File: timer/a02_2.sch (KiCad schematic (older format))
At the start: 6 parts, among them U11 74HC27, U12 74HC02, U13 74HC02, U14 74HC02, U15 74HC02, U16 74HC02

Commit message: Added the start/stop logic to timer page A02-2, and introduced a new part, 74LVC07, that I think will be the solution for open drain things
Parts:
- added R1: 5k, symbol R
- added unit 3 of U11
- added unit 3 of U16
- added unit 4 of U16
- added U19: 74HC27, symbol 74HC27
- added U20: 74LVC07, symbol 74LVC07
- added U21: 74HC04, symbol 74HC04
- added U22, U23: 74HC02, symbol 74HC02
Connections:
- net GND: now also U11.7 (GND), U16.7 (GND), U16.7 (GND), U19.7 (GND), U19.7 (GND), U19.7 (GND), U20.7 (GND), U20.7 (GND), U21.7 (GND), U21.7 (GND), U21.7 (GND), U21.7 (GND), U21.7 (GND), U21.7 (GND), U22.7 (GND), U22.7 (GND), U22.7 (GND), U23.7 (GND), U23.7 (GND), U23.7 (GND), U23.7 (GND)
- net VCC: now also R1.1, U11.14 (VCC), U16.14 (VCC), U16.14 (VCC), U19.14 (VCC), U19.14 (VCC), U19.14 (VCC), U20.14 (VCC), U20.14 (VCC), U21.14 (VCC), U21.14 (VCC), U21.14 (VCC), U21.14 (VCC), U21.14 (VCC), U21.14 (VCC), U22.14 (VCC), U22.14 (VCC), U22.14 (VCC), U23.14 (VCC), U23.14 (VCC), U23.14 (VCC), U23.14 (VCC)
- new net: U19.12, U20.1
- new net: R1.2, U11.10, U16.8, U20.2, U20.4, U21.1
- new net: U19.6, U20.3
- new net: U16.10, U19.5
- new net: U16.12, U21.2
- new net: U11.8, U23.2
- new net: U19.10, U21.4
- new net: U19.8, U23.8
- new net: U16.13, U23.6
- new net: U22.1, U23.12
- new net: U23.1, U23.5
- new net: U23.10, U23.11
- new net: U22.9, U23.13, U23.9
- new net ALGA: U19.2
- new net EVNSET/: U11.11, U16.11, U19.11, U22.2
- new net GOJ1: U16.9
- new net GOJAM: U21.6, U21.9
- new net GOJAM/: U21.5, U22.4
- new net MGOJAM: U21.8
- new net MSTP: U21.3, U22.3
- new net MSTPIT/: U21.12
- new net MSTRTP: U19.13
- new net SBY: U19.1
- new net STOP: U21.10, U21.13
- new net STOP/: U21.11, U22.10
- new net STOPA: U22.6, U22.8, U23.3, U23.4
- new net STRT1: U19.3
- new net STRT2: U19.4, U22.5
- new net T12DC/: U11.9, U19.9
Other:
- note added: "First stage of the scaler. This should maybe be moved to the scaler module?\nIt probably makes more sense there."
- note added: "Start/Stop Logic"
- note added: "TODO: Add descriptive local net names to this for debugging"

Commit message: Filled out the rest of page A03-1. At the very least, it appears to be properly handling the GOJAM condition. Haven't looked much at non-GOJAM behavior. I also exposed T01..T12 and T01/..T12/ as outputs of the timer module. I'm going to need a bigger (or another) connector there soon
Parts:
- U23: Initial (none) -> 1
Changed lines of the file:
@@
 F 2 "" H 13450 4550 60  0000 C CNN
 F 3 "" H 13450 4550 60  0000 C CNN
+F 4 "1" H 13700 4550 60  0000 C CIN "Initial"
 	1    13450 4550
 	1    0    0    -1
@@
 F 2 "" H 13450 5850 60  0000 C CNN
 F 3 "" H 13450 5850 60  0000 C CNN
+F 4 "1" H 13700 5850 60  0000 C CIN "Initial"
 	3    13450 5850
 	1    0    0    -1

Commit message: Renamed components in the timer module to fit the new numbering scheme (module_number * 1000 + part number), and updated initial conditions to make simulation happy again after fixes
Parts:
- renumbered R1 to R2001, U11 to U2011, U12 to U2012, U13 to U2013, U14 to U2014, U15 to U2015, U16 to U2016, U19 to U2019, U21 to U2021, U22 to U2022, U23 to U2023

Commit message: Added the 'stage' bit of the Stage Branch Decoder module, and cleaned up a lot of initial conditions (still probably a lot to be done there)
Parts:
- U2016, U2023: Initial 1 -> (none)
- U2019, U2021, U2023: Initial (none) -> 1
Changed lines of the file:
@@
 F 2 "" H 8400 4850 60  0000 C CNN
 F 3 "" H 8400 4850 60  0000 C CNN
+F 4 "1" H 8650 4850 60  0000 C CIN "Initial"
 	1    8400 4850
 	1    0    0    -1
@@
 F 2 "" H 8400 5350 60  0000 C CNN
 F 3 "" H 8400 5350 60  0000 C CNN
+F 4 "1" H 8650 5350 60  0000 C CIN "Initial"
 	2    8400 5350
 	1    0    0    -1
@@
 F 2 "" H 8400 6050 60  0000 C CNN
 F 3 "" H 8400 6050 60  0000 C CNN
-F 4 "1" H 8600 6100 60  0000 C CIN "Initial"
 	3    8400 6050
 	1    0    0    -1
@@
 F 2 "" H 10700 5350 60  0000 C CNN
 F 3 "" H 10700 5350 60  0000 C CNN
+F 4 "1" H 10700 5350 60  0001 C CNN "Initial"
 	1    10700 5350
 	1    0    0    -1
@@
 F 2 "" H 13450 4550 60  0000 C CNN
 F 3 "" H 13450 4550 60  0000 C CNN
-F 4 "1" H 13700 4550 60  0000 C CIN "Initial"
 	1    13450 4550
 	1    0    0    -1
@@
 F 2 "" H 13450 5250 60  0000 C CNN
 F 3 "" H 13450 5250 60  0000 C CNN
+F 4 "1" H 13700 5250 60  0000 C CIN "Initial"
 	2    13450 5250
 	1    0    0    -1
@@
 F 2 "" H 13450 5850 60  0000 C CNN
 F 3 "" H 13450 5850 60  0000 C CNN
-F 4 "1" H 13700 5850 60  0000 C CIN "Initial"
 	3    13450 5850
 	1    0    0    -1
@@
 F 2 "" H 13450 6550 60  0000 C CNN
 F 3 "" H 13450 6550 60  0000 C CNN
+F 4 "1" H 13700 6550 60  0000 C CIN "Initial"
 	4    13450 6550
 	1    0    0    -1
@@
 F 2 "" H 16200 4450 60  0000 C CNN
 F 3 "" H 16200 4450 60  0000 C CNN
+F 4 "1" H 16250 4450 60  0000 C CIN "Initial"
 	3    16200 4450
 	1    0    0    -1
@@
 F 2 "" H 16200 5350 60  0000 C CNN
 F 3 "" H 16200 5350 60  0000 C CNN
+F 4 "1" H 16250 5350 60  0000 C CIN "Initial"
 	5    16200 5350
 	1    0    0    -1

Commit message: Added the strobe pulses to the timer
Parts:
- removed unit 1 of U2014
- added U2002, U2007: 74HC27, symbol 74HC27
- added U2004, U2037: 74HC02, symbol 74HC02
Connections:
- net GND: now also U2002.7 (GND), U2004.7 (GND), U2007.7 (GND), U2037.7 (GND), U2037.7 (GND), U2037.7 (GND)
- net P02: now also U2002.9, U2037.12
- net P02/: now also U2004.8, U2037.5
- net P03: now also U2007.8
- net P03/: now also U2002.10, U2007.11, U2037.9
- net P04: now also U2002.11, U2004.9
- net P05: now also U2037.6
- net P05/: now also U2037.11, U2037.8
- net VCC: now also U2002.14 (VCC), U2004.14 (VCC), U2007.14 (VCC), U2037.14 (VCC), U2037.14 (VCC), U2037.14 (VCC)
- net at U2013.10: now also U2007.10
- new net EDSET: U2002.8, U2007.9
- new net SB0: U2037.4
- new net SB1: U2037.10
- new net SB2: U2037.13
- new net SB4: U2004.10
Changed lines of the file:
@@
-$Comp
-L 74HC02 U2014
-U 1 1 56272343
-P 8950 1700
-F 0 "U2014" H 8950 1750 60  0000 C CNN
-F 1 "74HC02" H 9000 1650 60  0000 C CNN
-F 2 "" H 8950 1700 60  0000 C CNN
-F 3 "" H 8950 1700 60  0000 C CNN
-	1    8950 1700
-	1    0    0    -1
-$EndComp
 $Comp
 L 74HC02 U2014
@@
 	5750 2300 5750 2150
 Wire Wire Line
-	5750 2150 6950 1950
-Wire Wire Line
-	6950 1950 6950 900
+	6950 1950 5750 2150
+Wire Wire Line
+	6950 900  6950 1950
 Wire Wire Line
 	7050 1800 6950 1800
@@
 Connection ~ 6950 2300
 Wire Wire Line
-	8250 1700 8300 1700
-Wire Wire Line
-	8300 1700 8300 1600
-Wire Wire Line
-	8300 1600 8350 1600
+	8250 1700 8350 1700
 Wire Wire Line
 	8250 2400 8300 2400
@@
 	9550 2150 8350 1950
 Wire Wire Line
-	8350 1950 8350 1800
+	8350 1950 8350 1850
 Wire Wire Line
 	9550 900  9550 1950
@@
 Connection ~ 1300 1400
 Wire Wire Line
-	4350 900  4450 900
+	4350 900  4600 900
 Connection ~ 4350 1700
 Wire Wire Line
-	4350 3200 4450 3200
+	4350 3200 4650 3200
 Connection ~ 4350 2400
 Wire Wire Line
-	6950 900  7050 900
+	6950 900  7150 900
 Connection ~ 6950 1700
 Wire Wire Line
-	6950 3200 7050 3200
+	6950 3200 7250 3200
 Connection ~ 6950 2400
 Wire Wire Line
-	9550 900  9650 900
+	9550 900  9800 900
 Connection ~ 9550 1700
 Wire Wire Line
-	9550 3200 9650 3200
+	9550 3200 9800 3200
 Connection ~ 9550 2400
 Wire Wire Line
-	12150 900  12250 900
+	12150 900  12350 900
 Connection ~ 12150 1200
 Wire Wire Line
-	12150 3200 12250 3200
+	12150 3200 12400 3200
 Connection ~ 12150 2900
 Wire Wire Line
-	14750 900  14850 900
+	14750 900  15050 900
 Connection ~ 14750 1100
 Wire Wire Line
-	14750 3200 14850 3200
+	14750 3200 15000 3200
 Connection ~ 14750 3000
-Text HLabel 4450 900  2    60   Output ~ 0
+Text HLabel 4600 900  2    60   Output ~ 0
 P01
-Text HLabel 4450 3200 2    60   Output ~ 0
+Text HLabel 4650 3200 2    60   Output ~ 0
 P01/
-Text HLabel 7050 900  2    60   Output ~ 0
+Text HLabel 7150 900  2    60   Output ~ 0
 P02
-Text HLabel 7050 3200 2    60   Output ~ 0
+Text HLabel 7250 3200 2    60   Output ~ 0
 P02/
-Text HLabel 9650 900  2    60   Output ~ 0
+Text HLabel 9800 900  2    60   Output ~ 0
 P03
-Text HLabel 9650 3200 2    60   Output ~ 0
+Text HLabel 9800 3200 2    60   Output ~ 0
 P03/
-Text HLabel 12250 900  2    60   Output ~ 0
+Text HLabel 12350 900  2    60   Output ~ 0
 P04
-Text HLabel 12250 3200 2    60   Output ~ 0
+Text HLabel 12400 3200 2    60   Output ~ 0
 P04/
-Text HLabel 14850 900  2    60   Output ~ 0
+Text HLabel 15050 900  2    60   Output ~ 0
 P05
-Text HLabel 14850 3200 2    60   Output ~ 0
+Text HLabel 15000 3200 2    60   Output ~ 0
 P05/
 $Sheet
@@
 Text Notes 11750 3950 0    60   ~ 0
 TODO: Add descriptive local net names to this for debugging
+$Comp
+L 74HC02 U2037
+U 2 1 5637F41F
+P 16900 1050
+F 0 "U2037" H 16900 1100 60  0000 C CNN
+F 1 "74HC02" H 16950 1000 60  0000 C CNN
+F 2 "" H 16900 1050 60  0000 C CNN
+F 3 "" H 16900 1050 60  0000 C CNN
+	2    16900 1050
+	1    0    0    -1
+$EndComp
+Text Label 7000 3200 0    60   ~ 0
+P02/
+Wire Wire Line
+	16300 950  16050 950
+Text Label 16050 950  0    60   ~ 0
+P02/
+Text Label 14800 900  0    60   ~ 0
+P05
+Wire Wire Line
+	16300 1150 16050 1150
+Text Label 16050 1150 0    60   ~ 0
+P05
+Text HLabel 17650 1050 2    60   Output ~ 0
+SB0
+Wire Wire Line
+	17650 1050 17500 1050
+$Comp
+L 74HC02 U2037
+U 3 1 563841F5
+P 16900 1550
+F 0 "U2037" H 16900 1600 60  0000 C CNN
+F 1 "74HC02" H 16950 1500 60  0000 C CNN
+F 2 "" H 16900 1550 60  0000 C CNN
+F 3 "" H 16900 1550 60  0000 C CNN
+	3    16900 1550
+	1    0    0    -1
+$EndComp
+$Comp
+L 74HC02 U2037
+U 4 1 563842BE
+P 16900 2050
+F 0 "U2037" H 16900 2100 60  0000 C CNN
+F 1 "74HC02" H 16950 2000 60  0000 C CNN
+F 2 "" H 16900 2050 60  0000 C CNN
+F 3 "" H 16900 2050 60  0000 C CNN
+	4    16900 2050
+	1    0    0    -1
+$EndComp
+$Comp
+L 74HC02 U2004
+U 3 1 5638520D
+P 16900 2550
+F 0 "U2004" H 16900 2600 60  0000 C CNN
+F 1 "74HC02" H 16950 2500 60  0000 C CNN
+F 2 "" H 16900 2550 60  0000 C CNN
+F 3 "" H 16900 2550 60  0000 C CNN
+	3    16900 2550
+	1    0    0    -1
+$EndComp
+Wire Wire Line
+	17500 1550 17650 1550
+Text HLabel 17650 1550 2    60   Output ~ 0
+SB1
+Text HLabel 17650 2050 2    60   Output ~ 0
+SB2
+Wire Wire Line
+	17650 2050 17500 2050
+Text HLabel 17650 2550 2    60   Output ~ 0
+SB4
+Wire Wire Line
+	17650 2550 17500 2550
+Wire Wire Line
+	16300 1450 16050 1450
+Wire Wire Line
+	16300 1650 16050 1650
+Wire Wire Line
+	16300 1950 16050 1950
+Wire Wire Line
+	16300 2150 16050 2150
+Wire Wire Line
+	16300 2450 16050 2450
+Wire Wire Line
+	16300 2650 16050 2650
+Text Label 16050 1450 0    60   ~ 0
+P05/
+Text Label 16050 1650 0    60   ~ 0
+P03/
+Text Label 16050 1950 0    60   ~ 0
+P05/
+Text Label 16050 2150 0    60   ~ 0
+P02
+Text Label 16050 2450 0    60   ~ 0
+P02/
+Text Label 16050 2650 0    60   ~ 0
+P04
+$Comp
+L 74HC27 U2002
+U 3 1 56386C94
+P 16900 3050
+F 0 "U2002" H 16900 3100 60  0000 C CNN
+F 1 "74HC27" H 16900 3000 60  0000 C CNN
+F 2 "" H 16900 3050 60  0000 C CNN
+F 3 "" H 16900 3050 60  0000 C CNN
+	3    16900 3050
+	1    0    0    -1
+$EndComp
+Text HLabel 17650 3050 2    60   Output ~ 0
+EDSET
+Wire Wire Line
+	17650 3050 17500 3050
+Wire Wire Line
+	16300 2900 16050 2900
+Wire Wire Line
+	16050 3050 16300 3050
+Wire Wire Line
+	16050 3200 16300 3200
+Text Label 16050 2900 0    60   ~ 0
+P02
+Text Label 16050 3050 0    60   ~ 0
+P03/
+Text Label 16050 3200 0    60   ~ 0
+P04
+Text Label 6950 900  0    60   ~ 0
+P02
+Text Label 14750 3200 0    60   ~ 0
+P05/
+Text Label 12150 900  0    60   ~ 0
+P04
+Text Label 12150 3200 0    60   ~ 0
+P04/
+Text Label 9550 3200 0    60   ~ 0
+P03/
+Text Label 9550 900  0    60   ~ 0
+P03
+Text Label 4350 900  0    60   ~ 0
+P01
+Text Label 4400 3200 0    60   ~ 0
+P01/
+$Comp
+L 74HC27 U2007
+U 3 1 5636CD8C
+P 8950 1700
+F 0 "U2007" H 8950 1750 60  0000 C CNN
+F 1 "74HC27" H 8950 1650 60  0000 C CNN
+F 2 "" H 8950 1700 60  0000 C CNN
+F 3 "" H 8950 1700 60  0000 C CNN
+	3    8950 1700
+	1    0    0    -1
+$EndComp
+Wire Wire Line
+	17600 3050 17600 3400
+Wire Wire Line
+	17600 3400 15600 3400
+Wire Wire Line
+	15600 3400 15600 600
+Wire Wire Line
+	15600 600  8250 600
+Wire Wire Line
+	8250 600  8250 1550
+Wire Wire Line
+	8250 1550 8350 1550
+Connection ~ 17600 3050
 $EndSCHEMATC

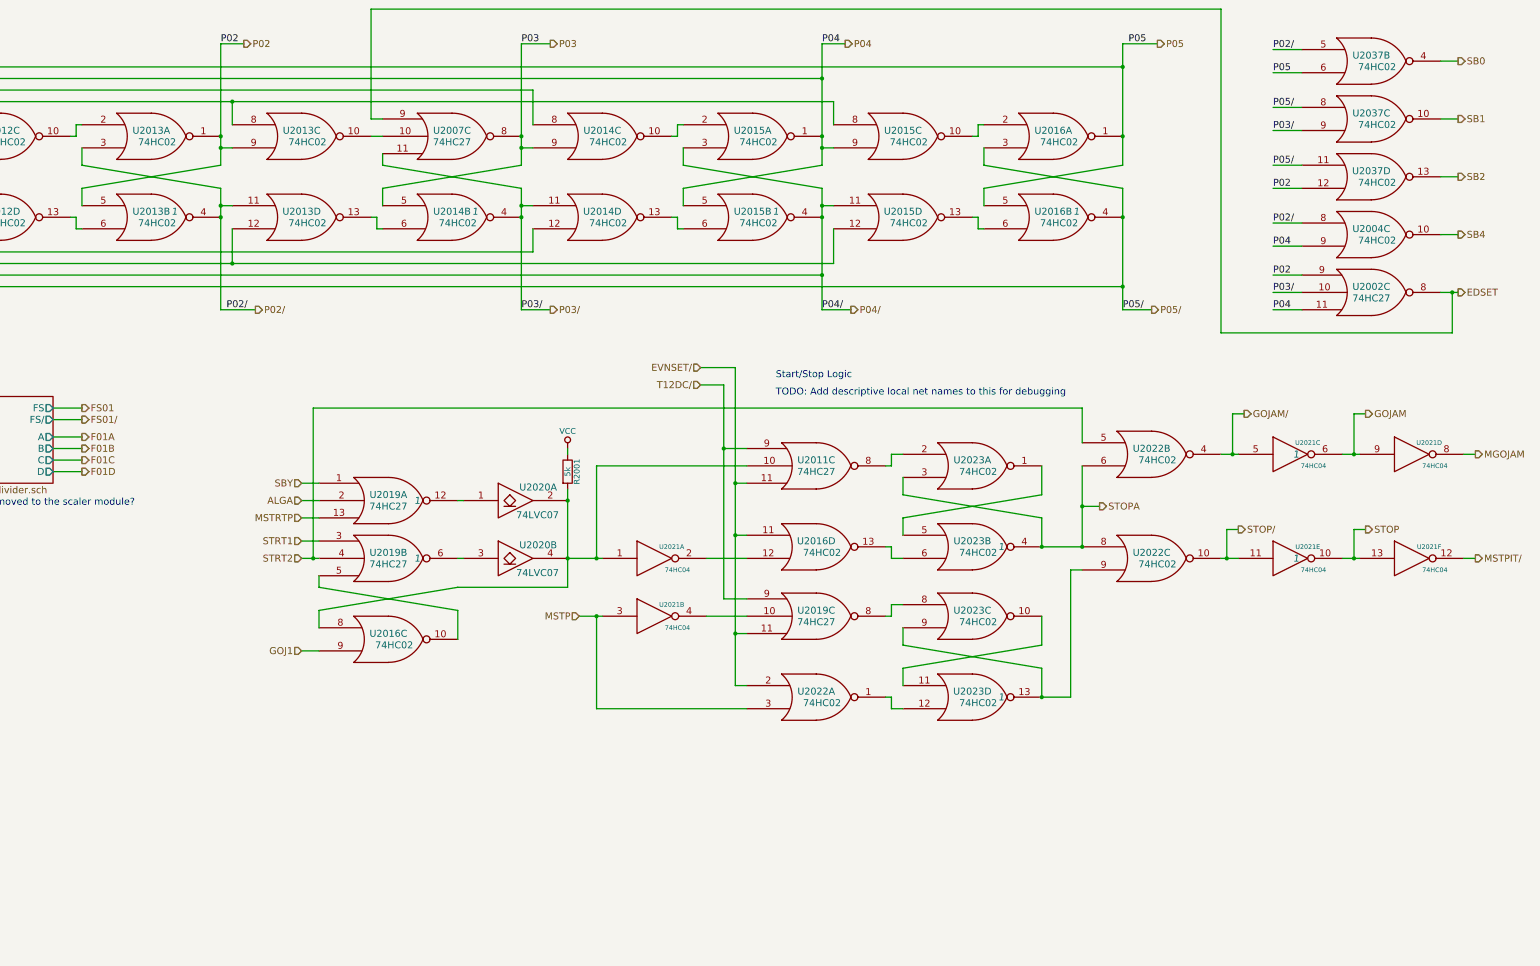
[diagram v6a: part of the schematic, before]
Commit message: First page of module A06, crosspoint generator #2.
There's a lot of gates I left out that produce unused (monitor?)
signals... namely the S01..S07/ -> IL01..IL07/ mappings, and the
RSTK/ -> RSTKX/ + RSTKY/ things. I also moved what looks like additional
timer logic to page 2 of the timer module (it's a really good fit there
because no new input pins are needed, all involved signals are generated
on that page).
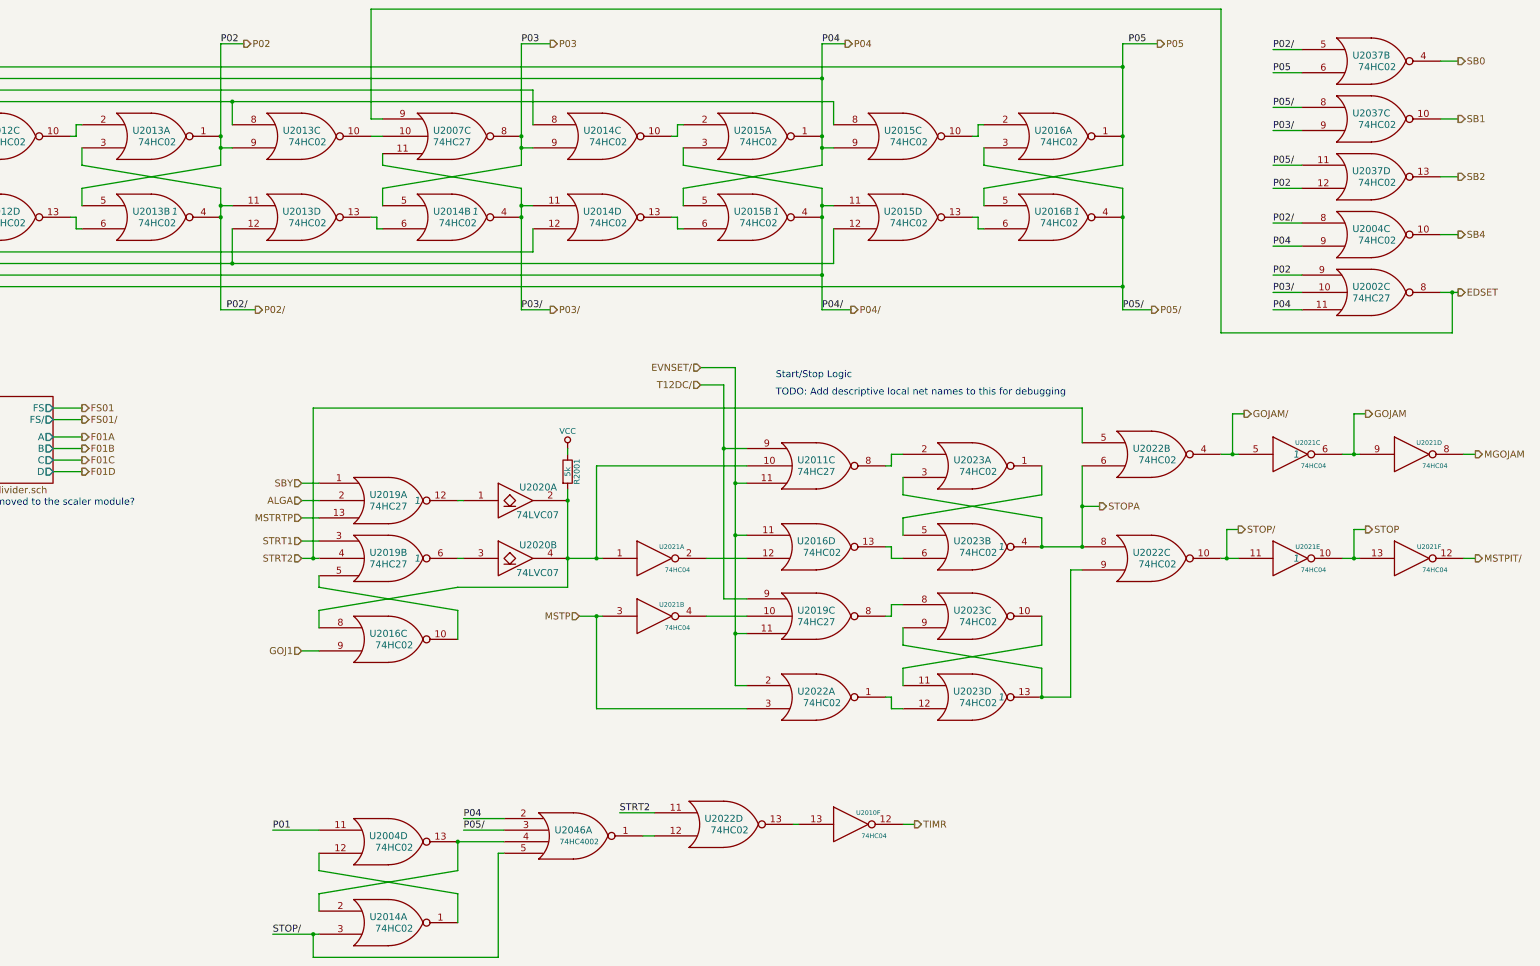
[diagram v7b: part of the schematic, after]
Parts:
- added unit 4 of U2004
- added U2010: 74HC04, symbol 74HC04
- added unit 1 of U2014
- added unit 4 of U2022
- added U2046: 74HC4002, symbol 74HC4002
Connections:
- net GND: now also U2004.7 (GND), U2010.7 (GND), U2014.7 (GND), U2022.7 (GND), U2046.7 (GND)
- net P01: now also U2004.11
- net P04: now also U2046.2
- net P05/: now also U2046.3
- net STOP/: now also U2014.3, U2046.5
- net STRT2: now also U2022.11
- net VCC: now also U2004.14 (VCC), U2010.14 (VCC), U2014.14 (VCC), U2022.14 (VCC), U2046.14 (VCC)
- new net: U2004.12, U2014.1
- new net: U2004.13, U2014.2, U2046.4
- new net: U2022.12, U2046.1
- new net: U2010.13, U2022.13
- new net TIMR: U2010.12
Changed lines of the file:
@@
 	5750 2300 5750 2150
 Wire Wire Line
-	6950 1950 5750 2150
-Wire Wire Line
-	6950 900  6950 1950
+	5750 2150 6950 1950
+Wire Wire Line
+	6950 1950 6950 900
 Wire Wire Line
 	7050 1800 6950 1800
@@
 EDSET
 Wire Wire Line
-	17650 3050 17500 3050
+	17500 3050 17650 3050
 Wire Wire Line
 	16300 2900 16050 2900
@@
 	8250 1550 8350 1550
 Connection ~ 17600 3050
+$Comp
+L 74HC02 U2004
+U 4 1 5694EFF5
+P 8400 7800
+F 0 "U2004" H 8400 7850 60  0000 C CNN
+F 1 "74HC02" H 8450 7750 60  0000 C CNN
+F 2 "" H 8400 7800 60  0000 C CNN
+F 3 "" H 8400 7800 60  0000 C CNN
+	4    8400 7800
+	1    0    0    -1
+$EndComp
+$Comp
+L 74HC02 U2014
+U 1 1 5694F276
+P 8400 8500
+F 0 "U2014" H 8400 8550 60  0000 C CNN
+F 1 "74HC02" H 8450 8450 60  0000 C CNN
+F 2 "" H 8400 8500 60  0000 C CNN
+F 3 "" H 8400 8500 60  0000 C CNN
+	1    8400 8500
+	1    0    0    -1
+$EndComp
+Wire Wire Line
+	9000 8500 9000 8250
+Wire Wire Line
+	9000 8250 7800 8050
+Wire Wire Line
+	7800 8050 7800 7900
+Wire Wire Line
+	9000 7800 9000 8050
+Wire Wire Line
+	9000 8050 7800 8250
+Wire Wire Line
+	7800 8250 7800 8400
+Wire Wire Line
+	7800 7700 7400 7700
+Wire Wire Line
+	7400 8600 7800 8600
+$Comp
+L 74HC4002 U2046
+U 1 1 569519D8
+P 10000 7750
+F 0 "U2046" H 10000 7800 60  0000 C CNN
+F 1 "74HC4002" H 10050 7700 47  0000 C CNN
+F 2 "" H 10000 7750 60  0000 C CNN
+F 3 "" H 10000 7750 60  0000 C CNN
+	1    10000 7750
+	1    0    0    -1
+$EndComp
+Wire Wire Line
+	9000 7800 9400 7800
+Connection ~ 9000 7800
+Wire Wire Line
+	7750 8600 7750 8800
+Wire Wire Line
+	7750 8800 9350 8800
+Wire Wire Line
+	9350 8800 9350 7900
+Wire Wire Line
+	9350 7900 9400 7900
+Connection ~ 7750 8600
+Wire Wire Line
+	9400 7700 9050 7700
+Text Label 7400 7700 0    60   ~ 0
+P01
+Text Label 7400 8600 0    60   ~ 0
+STOP/
+Text Label 9050 7700 0    60   ~ 0
+P05/
+Wire Wire Line
+	9400 7600 9050 7600
+Text Label 9050 7600 0    60   ~ 0
+P04
+$Comp
+L 74HC02 U2022
+U 4 1 56955F28
+P 11300 7650
+F 0 "U2022" H 11300 7700 60  0000 C CNN
+F 1 "74HC02" H 11350 7600 60  0000 C CNN
+F 2 "" H 11300 7650 60  0000 C CNN
+F 3 "" H 11300 7650 60  0000 C CNN
+	4    11300 7650
+	1    0    0    -1
+$EndComp
+Wire Wire Line
+	10600 7750 10700 7750
+Wire Wire Line
+	10700 7550 10400 7550
+Text Label 10400 7550 0    60   ~ 0
+STRT2
+$Comp
+L 74HC04 U2010
+U 6 1 56956CDF
+P 12400 7650
+F 0 "U2010" H 12550 7750 40  0000 C CNN
+F 1 "74HC04" H 12600 7550 40  0000 C CNN
+F 2 "" H 12400 7650 60  0000 C CNN
+F 3 "" H 12400 7650 60  0000 C CNN
+	6    12400 7650
+	1    0    0    -1
+$EndComp
+Wire Wire Line
+	11900 7650 11950 7650
+Wire Wire Line
+	12850 7650 12950 7650
+Text HLabel 12950 7650 2    60   Output ~ 0
+TIMR
 $EndSCHEMATC
